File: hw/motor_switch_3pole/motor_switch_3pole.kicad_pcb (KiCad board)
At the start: 2 copper layers, 50 x 50 mm, 48 parts, among them J1 WAGO 2081-1123, J2 WAGO 233-506, J3 CONN-ISP-6, J4 WAGO 243-723, J5 WAGO 243-724, J6 WAGO 243-721, J7 WAGO 243-722, Q1 BSS138, Q2 BSS138, U1 25LC256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

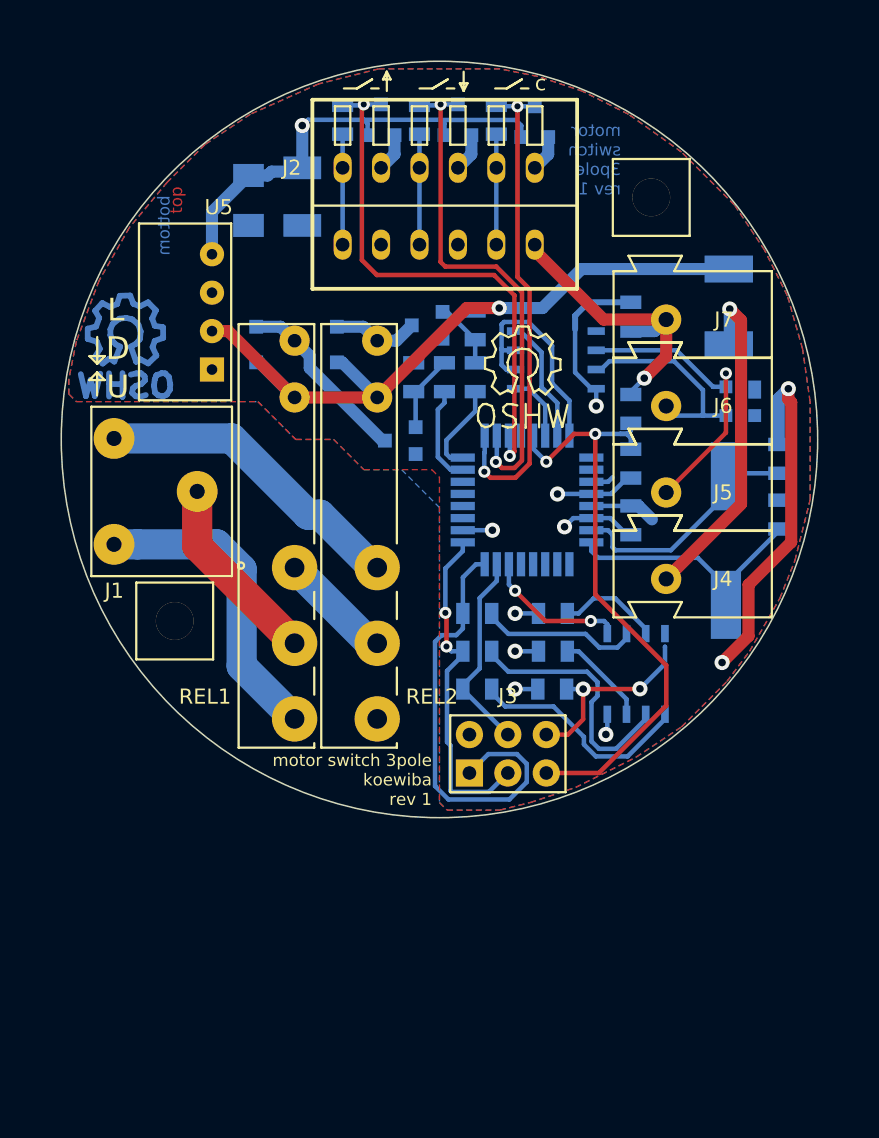
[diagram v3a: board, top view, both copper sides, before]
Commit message: Fixed relay pinout bug
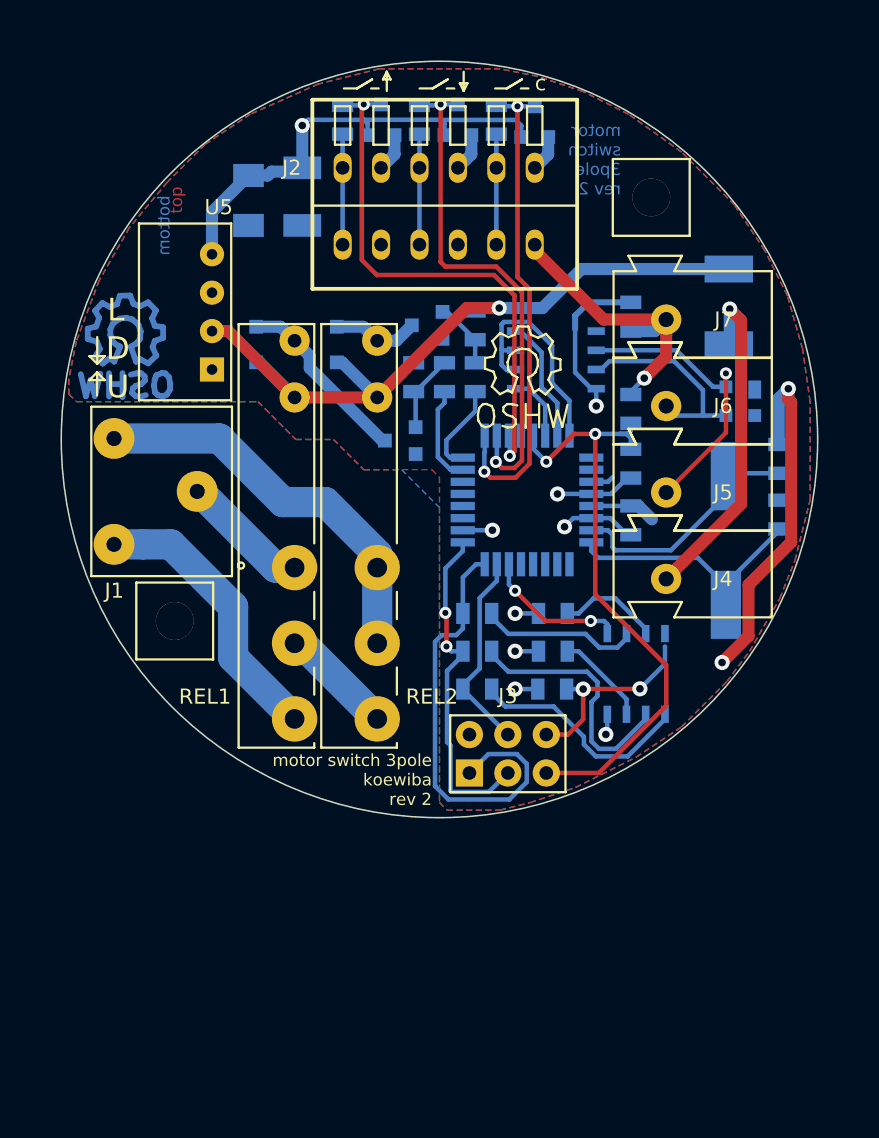
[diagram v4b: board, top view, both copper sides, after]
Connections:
- net /relay_on_off renamed /relay_on
- net /relay_up_down renamed /relay_up
- REL1 pad 3: /230V_ON -> /230V_DOWN
- REL1 pad 4: /230V_DOWN -> /230V_ON
- REL2 pad 4: /230V_ON -> /230V_L
- REL2 pad 5: (no net) -> /230V_ON
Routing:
- net /230V_L: track 20.9 -> 27.2 mm
- net /230V_DOWN: track 12.8 -> 8.59 mm
- net /230V_UP: track 20.5 -> 18.7 mm
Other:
- board text added: "motor switch 3pole koewiba rev 2"
- board text added: "motor switch 3pole rev 2"
- board text removed: "motor switch 3pole koewiba rev 1"
- board text removed: "motor switch 3pole rev 1"
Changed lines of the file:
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@@
-(kicad_pcb (version 20160815) (host pcbnew 4.1.0-alpha+201608281546+7098~46~ubuntu14.04.1-product)
+(kicad_pcb (version 20160815) (host pcbnew no-vcs-found)
   (general
-    (links 106)
+    (links 107)
     (no_connects 0)
-    (area 74.949999 74.949999 125.050001 125.050001)
+    (area 64 66.8 136.500001 134.745001)
     (thickness 1.6)
     (drawings 50)
-    (tracks 375)
+    (tracks 379)
     (zones 0)
     (modules 48)
@@
   (title_block
     (title "motor switch 3pole")
-    (date 2016-09-06)
-    (rev 1)
+    (date 2016-12-03)
+    (rev 2)
     (company koewiba)
   )
@@
     (visible_elements 7FFEFF7F)
     (pcbplotparams
-      (layerselection 0x01130_ffffffff)
+      (layerselection 0x011f0_ffffffff)
       (usegerberextensions false)
       (excludeedgelayer true)
@@
   (net 34 //button_down)
   (net 35 //switch_close)
-  (net 36 /relay_up_down)
-  (net 37 /relay_on_off)
+  (net 36 /relay_up)
+  (net 37 /relay_on)
   (net_class Default "This is the default net class."
     (clearance 0.2)
@@
     (add_net /bus_atmega328_basic/TXD0)
     (add_net /bus_atmega328_basic/TXD0EN)
-    (add_net /relay_on_off)
-    (add_net /relay_up_down)
+    (add_net /relay_on)
+    (add_net /relay_up)
     (add_net "Net-(C4-Pad1)")
     (add_net "Net-(C5-Pad1)")
@@
     (pad 22 smd rect (at 4.25 1.2 180) (size 1.6 0.55) (layers B.Cu B.Paste B.Mask))
     (pad 23 smd rect (at 4.25 2 180) (size 1.6 0.55) (layers B.Cu B.Paste B.Mask)
-      (net 36 /relay_up_down))
+      (net 36 /relay_up))
     (pad 24 smd rect (at 4.25 2.8 180) (size 1.6 0.55) (layers B.Cu B.Paste B.Mask)
-      (net 37 /relay_on_off))
+      (net 37 /relay_on))
     (pad 25 smd rect (at 2.8 4.25 90) (size 1.6 0.55) (layers B.Cu B.Paste B.Mask)
       (net 35 //switch_close))
@@
       (net 11 /230V_L))
     (pad 4 thru_hole circle (at 20 0 270) (size 3 3) (drill 1.3) (layers *.Cu *.Mask F.SilkS)
+      (net 11 /230V_L))
+    (pad 5 thru_hole circle (at 25 0 270) (size 3 3) (drill 1.3) (layers *.Cu *.Mask F.SilkS)
       (net 10 /230V_ON))
-    (pad 5 thru_hole circle (at 25 0 270) (size 3 3) (drill 1.3) (layers *.Cu *.Mask F.SilkS))
   )
   (module Relay:finder_34.51_1xUM (layer F.Cu)
@@
       (net 2 +24V))
     (pad 3 thru_hole circle (at 15 0 270) (size 3 3) (drill 1.3) (layers *.Cu *.Mask F.SilkS)
+      (net 9 /230V_DOWN))
+    (pad 4 thru_hole circle (at 20 0 270) (size 3 3) (drill 1.3) (layers *.Cu *.Mask F.SilkS)
       (net 10 /230V_ON))
-    (pad 4 thru_hole circle (at 20 0 270) (size 3 3) (drill 1.3) (layers *.Cu *.Mask F.SilkS)
-      (net 9 /230V_DOWN))
     (pad 5 thru_hole circle (at 25 0 270) (size 3 3) (drill 1.3) (layers *.Cu *.Mask F.SilkS)
       (net 8 /230V_UP))
@@
       (net 6 "Net-(Q1-Pad1)"))
     (pad 2 smd rect (at 0.9525 0 270) (size 0.889 1.397) (layers B.Cu B.Paste B.Mask)
-      (net 36 /relay_up_down))
+      (net 36 /relay_up))
     (model Resistors_SMD.3dshapes/R_0805.wrl
       (at (xyz 0 0 0))
@@
       (net 7 "Net-(Q2-Pad1)"))
     (pad 2 smd rect (at 0.9525 0 270) (size 0.889 1.397) (layers B.Cu B.Paste B.Mask)
-      (net 37 /relay_on_off))
+      (net 37 /relay_on))
     (model Resistors_SMD.3dshapes/R_0805.wrl
       (at (xyz 0 0 0))
@@
   (gr_line (start 125.5 100) (end 74.5 100) (layer Dwgs.User) (width 0.15))
   (gr_line (start 100 75) (end 100 125) (layer Dwgs.User) (width 0.15))
-  (gr_text "motor\nswitch\n3pole\nrev 1\n" (at 112 81.5) (layer B.Cu)
+  (gr_text "motor\nswitch\n3pole\nrev 2\n" (at 112 81.5) (layer B.Cu)
     (effects (font (size 0.8 0.8) (thickness 0.15)) (justify left mirror))
   )
@@
   (gr_line (start 96.52 75.692) (end 96.266 76.2) (layer F.SilkS) (width 0.15))
   (gr_line (start 96.52 76.962) (end 96.52 75.692) (layer F.SilkS) (width 0.15))
-  (gr_text "motor switch 3pole\nkoewiba\nrev 1\n" (at 99.5 122.5) (layer F.SilkS)
+  (gr_text "motor switch 3pole\nkoewiba\nrev 2\n" (at 99.5 122.5) (layer F.SilkS)
     (effects (font (size 0.8 0.8) (thickness 0.15)) (justify right))
   )
@@
   (segment (start 100.203 91.567) (end 100.5205 91.567) (width 0.3) (layer B.Cu) (net 7) (status 30))
   (segment (start 100.5205 91.567) (end 102.362 93.4085) (width 0.3) (layer B.Cu) (net 7) (status 30))
-  (segment (start 90.424 118.472) (end 86.923999 114.971999) (width 2) (layer B.Cu) (net 8))
-  (segment (start 86.923999 114.971999) (end 86.923999 108.58282) (width 2) (layer B.Cu) (net 8))
-  (segment (start 86.923999 108.58282) (end 85.275179 106.934) (width 2) (layer B.Cu) (net 8))
-  (segment (start 85.275179 106.934) (end 80.041634 106.934) (width 2) (layer B.Cu) (net 8))
-  (segment (start 80.041634 106.934) (end 78.486 106.934) (width 2) (layer B.Cu) (net 8))
-  (segment (start 90.424 113.472) (end 83.986 107.034) (width 2) (layer F.Cu) (net 9))
-  (segment (start 83.986 107.034) (end 83.986 103.434) (width 2) (layer F.Cu) (net 9))
+  (segment (start 90.424 118.472) (end 86.36 114.408) (width 2) (layer B.Cu) (net 8))
+  (segment (start 86.36 114.408) (end 86.36 111.049998) (width 2) (layer B.Cu) (net 8))
+  (segment (start 82.244002 106.934) (end 80.395188 106.934) (width 2) (layer B.Cu) (net 8))
+  (segment (start 80.395188 106.934) (end 78.486 106.934) (width 2) (layer B.Cu) (net 8))
+  (segment (start 86.36 111.049998) (end 82.244002 106.934) (width 2) (layer B.Cu) (net 8))
+  (segment (start 90.424 108.472) (end 89.168 108.472) (width 2) (layer B.Cu) (net 9))
+  (segment (start 89.168 108.472) (end 84.13 103.434) (width 2) (layer B.Cu) (net 9))
+  (segment (start 84.13 103.434) (end 83.986 103.434) (width 2) (layer B.Cu) (net 9))
   (segment (start 83.942965 103.477035) (end 83.986 103.434) (width 2) (layer B.Cu) (net 9) (status 30))
-  (segment (start 95.885 113.472) (end 95.424 113.472) (width 2) (layer B.Cu) (net 10) (status 30))
-  (segment (start 95.424 113.472) (end 90.424 108.472) (width 2) (layer B.Cu) (net 10) (status 30))
+  (segment (start 90.424 113.472) (end 90.885 113.472) (width 2) (layer B.Cu) (net 10))
+  (segment (start 90.885 113.472) (end 95.885 118.472) (width 2) (layer B.Cu) (net 10))
+  (segment (start 78.486 99.934) (end 85.444002 99.934) (width 2) (layer B.Cu) (net 11))
+  (segment (start 95.885 107.569) (end 95.885 108.472) (width 2) (layer B.Cu) (net 11))
+  (segment (start 85.444002 99.934) (end 89.650002 104.14) (width 2) (layer B.Cu) (net 11))
+  (segment (start 89.650002 104.14) (end 92.456 104.14) (width 2) (layer B.Cu) (net 11))
+  (segment (start 92.456 104.14) (end 95.885 107.569) (width 2) (layer B.Cu) (net 11))
+  (segment (start 95.885 113.472) (end 95.885 108.472) (width 2) (layer B.Cu) (net 11))
+  (segment (start 95.885 113.472) (end 95.424 113.472) (width 2) (layer B.Cu) (net 11) (status 30))
   (segment (start 95.885 108.472) (end 95.604002 108.472) (width 2) (layer B.Cu) (net 11))
-  (segment (start 86.268166 99.934) (end 78.486 99.934) (width 2) (layer B.Cu) (net 11))
-  (segment (start 95.604002 108.472) (end 92.104001 104.971999) (width 2) (layer B.Cu) (net 11))
-  (segment (start 92.104001 104.971999) (end 91.306165 104.971999) (width 2) (layer B.Cu) (net 11))
-  (segment (start 91.306165 104.971999) (end 86.268166 99.934) (width 2) (layer B.Cu) (net 11))
   (segment (start 110.041 106) (end 111.141 106) (width 0.3) (layer B.Cu) (net 12) (status 10))
   (segment (start 111.141 106) (end 111.4425 106.3015) (width 0.3) (layer B.Cu) (net 12))

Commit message: Update to KiCAD6: motor_switch_3pole
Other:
- net class 230V removed
- net class Default removed
- net class Power removed
